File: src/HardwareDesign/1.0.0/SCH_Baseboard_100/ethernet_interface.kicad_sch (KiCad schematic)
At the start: 1 part, among them J2 HR911105A

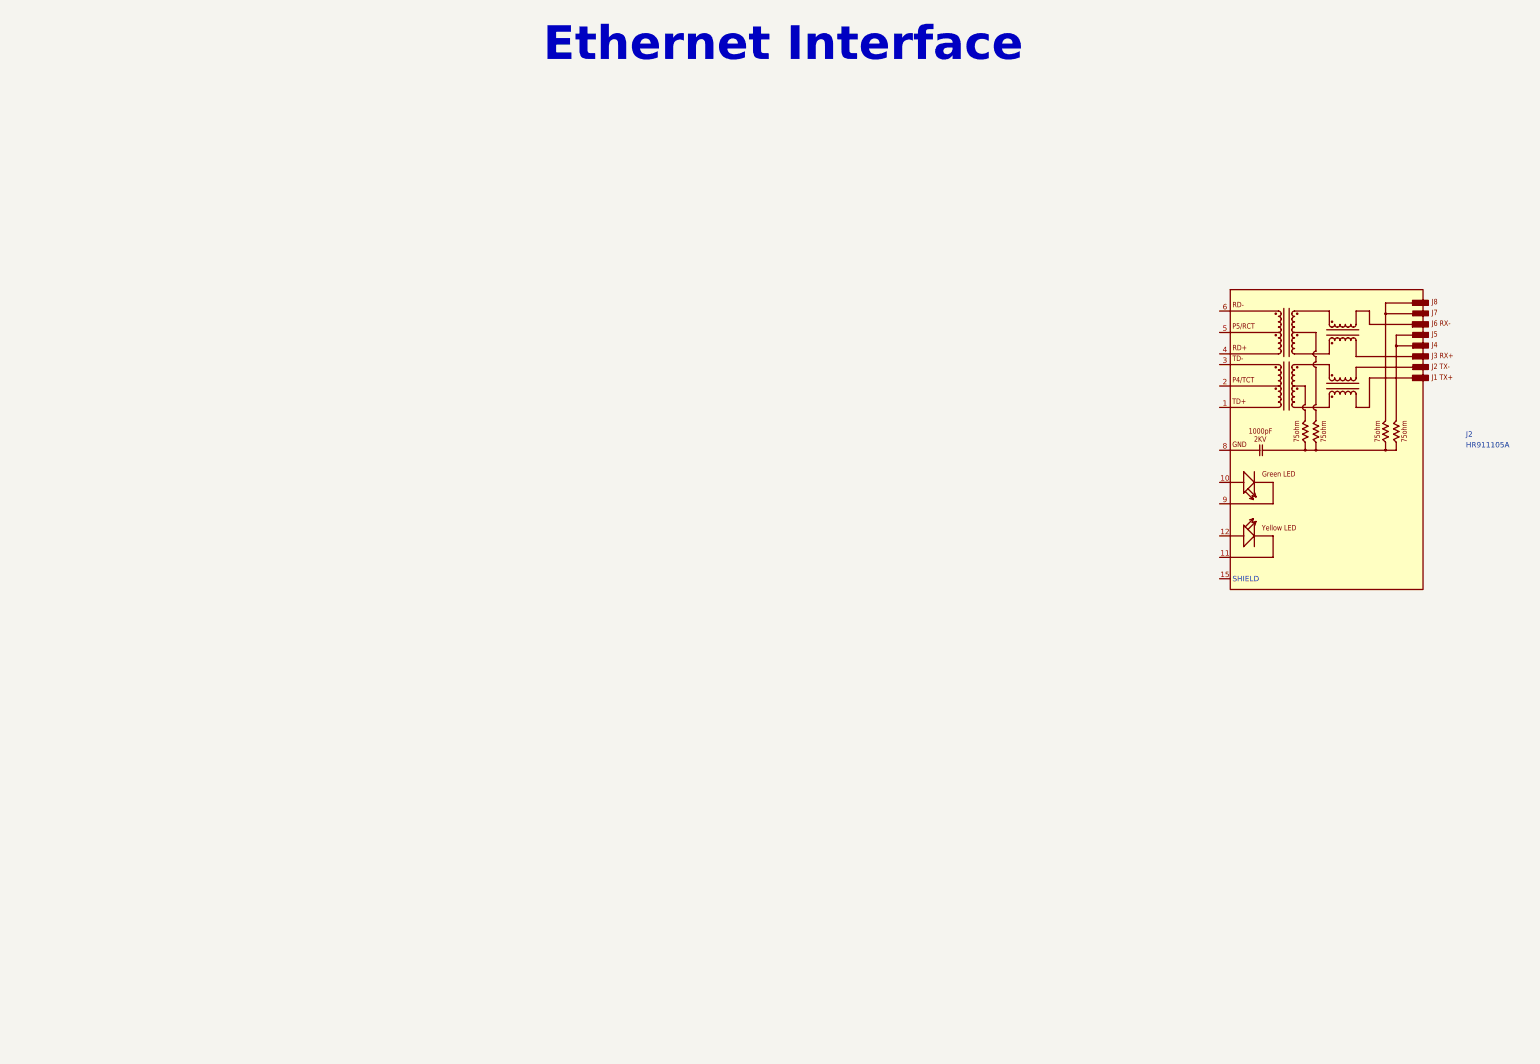
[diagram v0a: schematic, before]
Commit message: Add bladecore to design
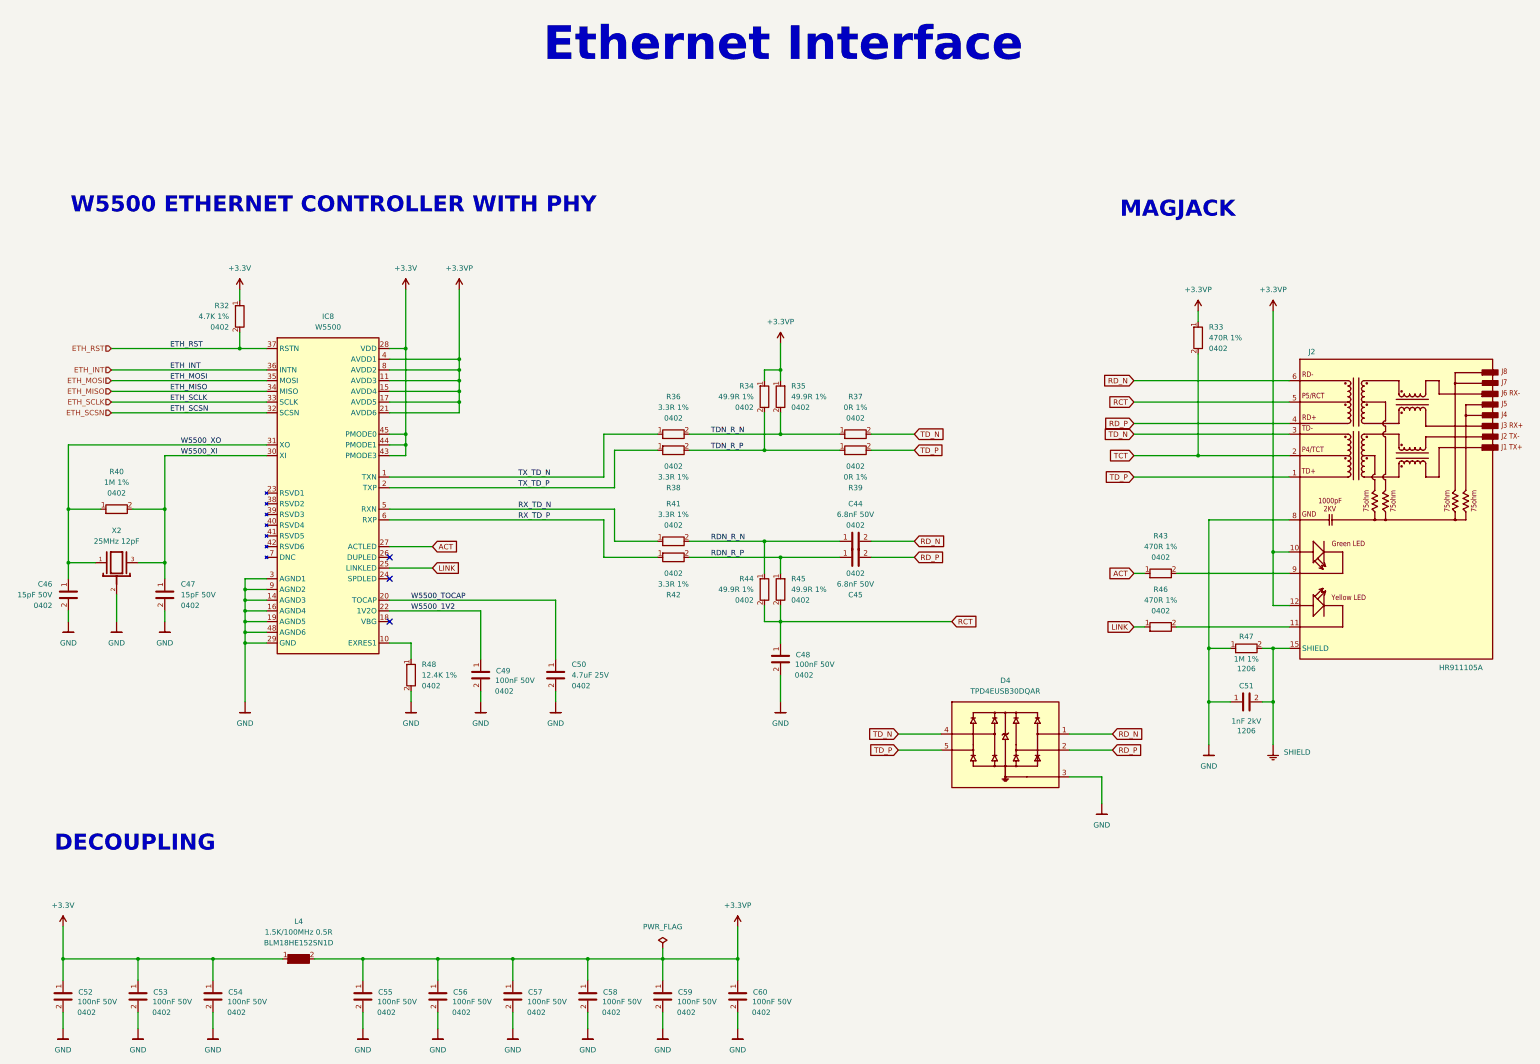
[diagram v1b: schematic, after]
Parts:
- added C44, C45: 6.8nF 50V, Capacitor_SMD:C_0402_1005Metric, symbol DS_Capacitor_0402:6.8nF 50V 0402
- added C46, C47: 15pF 50V, Capacitor_SMD:C_0402_1005Metric, symbol DS_Capacitor_0402:15pF 50V 0402
- added C48, C49, C52, C53, C54, C55, C56, C57, C58, C59, C60: 100nF 50V, Capacitor_SMD:C_0402_1005Metric, symbol DS_Capacitor_0402:100nF 50V 0402
- added C50: 4.7uF 25V, Capacitor_SMD:C_0402_1005Metric, symbol DS_Capacitor_0402:4.7uF 25V 0402
- added C51: 1nF 2kV, Capacitor_SMD:C_1206_3216Metric, symbol DS_Capacitor_1206:1nF 2kV 1206
- added D4: TPD4EUSB30DQAR, DS_Diode:USON10_2.5x1, symbol DS_Diode:TPD4EUSB30DQAR
- added IC8: W5500, DS_Peripherals:LQFP48_7x7, symbol DS_Peripherals:W5500
- added L4: 1.5K/100MHz 0.5R, Resistor_SMD:R_0603_1608Metric, symbol DS_Inductor:BLM18HE152SN1D
- added R32: 4.7K 1%, Resistor_SMD:R_0402_1005Metric, symbol DS_Resistor_0402:4.7K 1% 0402
- added R33, R43, R46: 470R 1%, Resistor_SMD:R_0402_1005Metric, symbol DS_Resistor_0402:470R 1% 0402
- added R34, R35, R44, R45: 49.9R 1%, Resistor_SMD:R_0402_1005Metric, symbol DS_Resistor_0402:49.9R 1% 0402
- added R36, R38, R41, R42: 3.3R 1%, Resistor_SMD:R_0402_1005Metric, symbol DS_Resistor_0402:3.3R 1% 0402
- added R37, R39: 0R 1%, Resistor_SMD:R_0402_1005Metric, symbol DS_Resistor_0402:0R 1% 0402
- added R40: 1M 1%, Resistor_SMD:R_0402_1005Metric, symbol DS_Resistor_0402:1M 1% 0402
- added R47: 1M 1%, Resistor_SMD:R_1206_3216Metric, symbol DS_Resistor_1206:1M 1% 1206
- added R48: 12.4K 1%, Resistor_SMD:R_0402_1005Metric, symbol DS_Resistor_0402:12.4K 1% 0402
- added X2: 25MHz 12pF, DS_Crystal:X3225, symbol DS_Crystal:25MHz
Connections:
- net TD_P: now reaches J2.1 (TD+)
- net TD_P: now also D4.5, R39.2
- net +3.3VP: now reaches J2.10 (GREEN+)
- net +3.3VP: now also J2.12 (YELLOW+), C55.1, C56.1, C57.1, C58.1, C59.1, C60.1, IC8.11 (AVDD3), IC8.15 (AVDD4), IC8.17 (AVDD5), IC8.21 (AVDD6), IC8.4 (AVDD1), IC8.8 (AVDD2), L4.2, R33.1, R34.1, R35.1
- net at J2.11 (YELLOW-): now also R46.2
- net SHIELD: now reaches J2.15 (SHIELD)
- net SHIELD: now also C51.2, R47.2
- net TCT: now reaches J2.2 (P4/TCT)
- net TCT: now also R33.2
- net TD_N: now reaches J2.3 (TD-)
- net TD_N: now also D4.4, R37.2
- net RD_P: now reaches J2.4 (RD+)
- net RD_P: now also C45.2, D4.2
- net RCT: now reaches J2.5 (P5/RCT)
- net RCT: now also C48.1, R44.2, R45.2
- net RD_N: now reaches J2.6 (RD-)
- net RD_N: now also C44.2, D4.1
- net GND: now reaches J2.8 (GND)
- net GND: now also C46.2, C47.2, C48.2, C49.2, C50.2, C51.1, C52.2, C53.2, C54.2, C55.2, C56.2, C57.2, C58.2, C59.2, C60.2, D4.3, IC8.14 (AGND3), IC8.16 (AGND4), IC8.19 (AGND5), IC8.29 (GND), IC8.3 (AGND1), IC8.48 (AGND6), IC8.9 (AGND2), R47.1, R48.2, X2.2
- net at J2.9 (GREEN-): now also R43.2
- new net: IC8.10 (EXRES1), R48.1
- new net +3.3V: C52.1, C53.1, C54.1, IC8.28 (VDD), IC8.43 (PMODE3), IC8.44 (PMODE1), IC8.45 (PMODE0), L4.1, R32.1
- new net ACT: IC8.27 (ACTLED), R43.1
- new net ETH_INT: IC8.36 (INTN)
- new net ETH_MISO: IC8.34 (MISO)
- new net ETH_MOSI: IC8.35 (MOSI)
- new net ETH_RST: IC8.37 (RSTN), R32.2
- new net ETH_SCLK: IC8.33 (SCLK)
- new net ETH_SCSN: IC8.32 (SCSN)
- new net LINK: IC8.25 (LINKLED), R46.1
- new net RDN_R_N: C44.1, R41.2, R44.1
- new net RDN_R_P: C45.1, R42.2, R45.1
- new net RX_TD_N: IC8.5 (RXN), R41.1
- new net RX_TD_P: IC8.6 (RXP), R42.1
- new net TDN_R_N: R35.2, R36.2, R37.1
- new net TDN_R_P: R34.2, R38.2, R39.1
- new net TX_TD_N: IC8.1 (TXN), R36.1
- new net TX_TD_P: IC8.2 (TXP), R38.1
- new net W5500_1V2: C49.1, IC8.22 (1V2O)
- new net W5500_TOCAP: C50.1, IC8.20 (TOCAP)
- new net W5500_XI: C47.1, IC8.30 (XI), R40.2, X2.3
- new net W5500_XO: C46.1, IC8.31 (XO), R40.1, X2.1
- no-connect marks 0 -> 3
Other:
- note added: "DECOUPLING"
- note added: "MAGJACK"
- note added: "W5500 ETHERNET CONTROLLER WITH PHY"
